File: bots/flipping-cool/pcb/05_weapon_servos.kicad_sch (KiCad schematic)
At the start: 6 parts, among them J30 SAVOX_SH0255MGP_FRONT_REAR_AX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, J31 SAVOX_SH0255MGP_LEFT_RIGHT_AX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, J32 SPARE_SERVO_PWM5, J33 SPARE_SERVO_PWM6

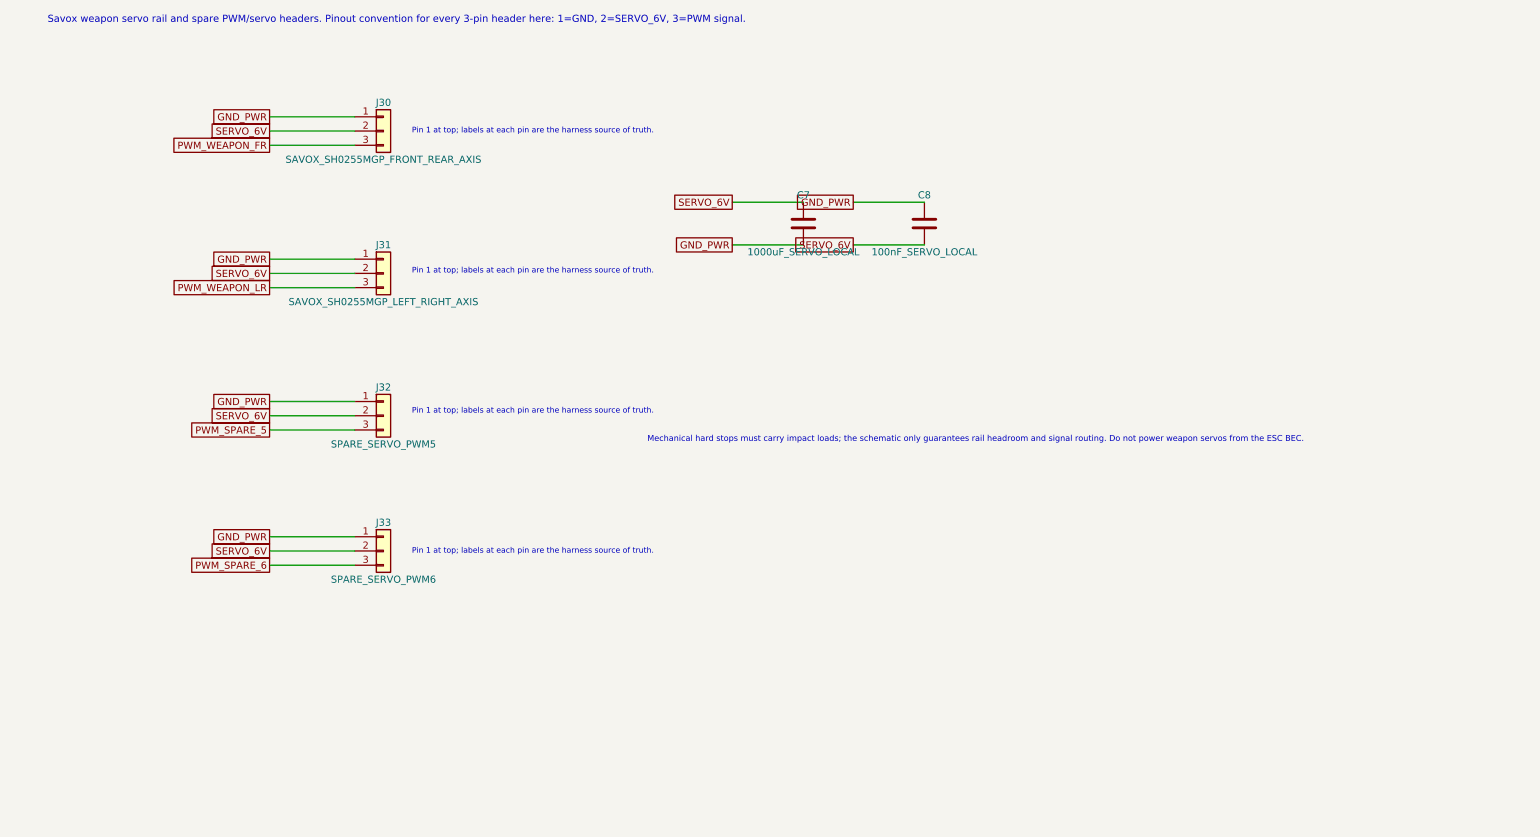
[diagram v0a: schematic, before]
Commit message: Refactor Flipping Cool PCB design to Rev B, updating title, date, and revision details. Integrate ESP32-S3 module and enhance documentation for MCU I/O and debugging features, while maintaining historical context from Rev A.
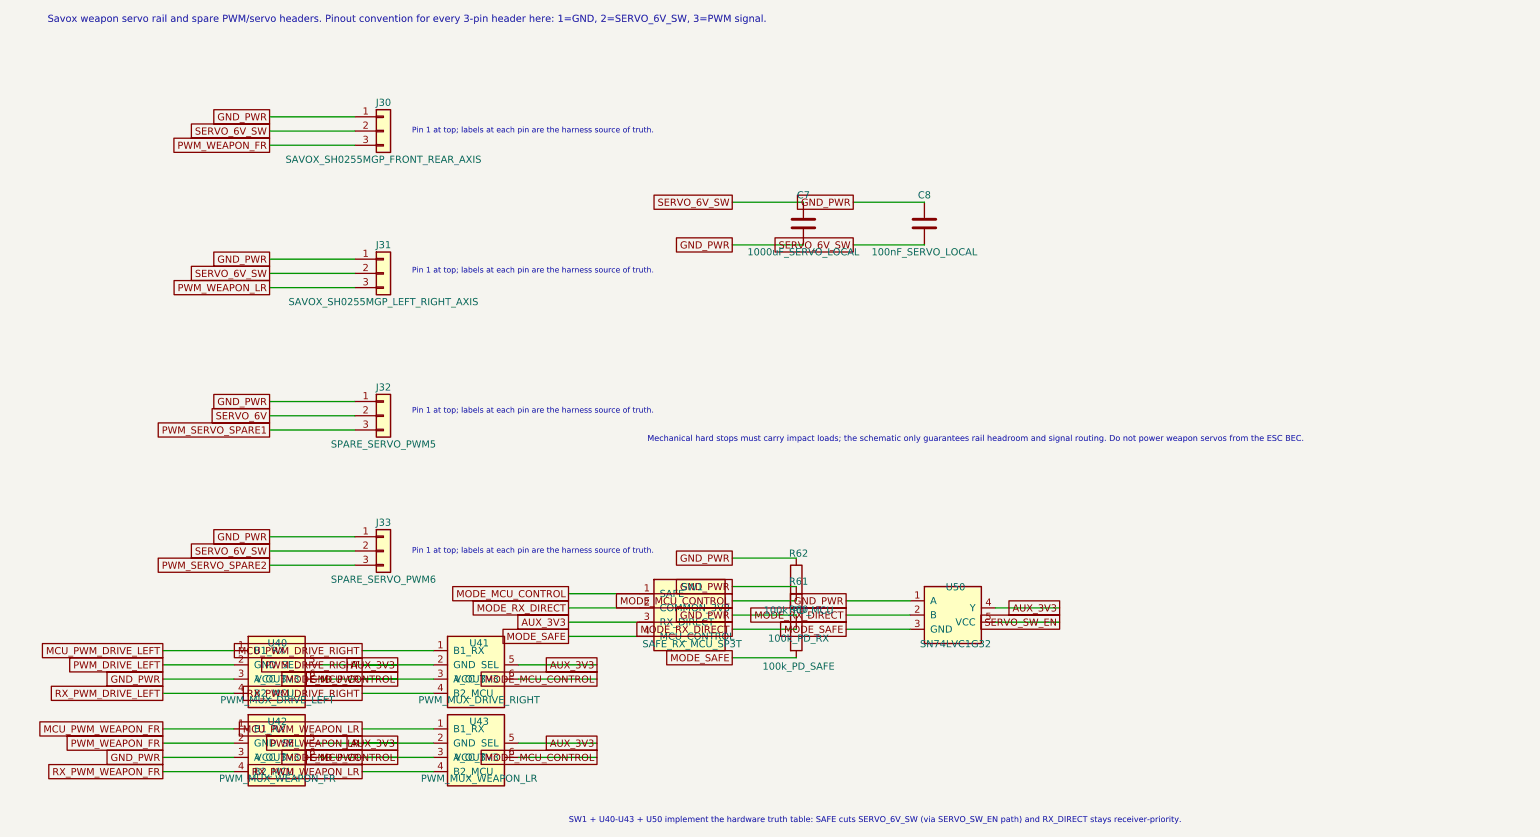
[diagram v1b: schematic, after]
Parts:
- added R60: 100k_PD_SAFE, Resistor_SMD:R_0805_2012Metric, symbol Device:R
- added R61: 100k_PD_RX, Resistor_SMD:R_0805_2012Metric, symbol Device:R
- added R62: 100k_PD_MCU, Resistor_SMD:R_0805_2012Metric, symbol Device:R
- added SW1: SAFE_RX_MCU_SP3T, Button_Switch_SMD:SW_SP3T_PCM13, symbol custom:MODE_SWITCH_SP3T_SAFE_RX_MCU
- added U40: PWM_MUX_DRIVE_LEFT, Package_TO_SOT_SMD:SOT-23-6, symbol custom:MUX_74LVC1G3157
- added U41: PWM_MUX_DRIVE_RIGHT, Package_TO_SOT_SMD:SOT-23-6, symbol custom:MUX_74LVC1G3157
- added U42: PWM_MUX_WEAPON_FR, Package_TO_SOT_SMD:SOT-23-6, symbol custom:MUX_74LVC1G3157
- added U43: PWM_MUX_WEAPON_LR, Package_TO_SOT_SMD:SOT-23-6, symbol custom:MUX_74LVC1G3157
- added U50: SN74LVC1G32, Package_TO_SOT_SMD:SOT-23-5, symbol custom:LOGIC_SN74LVC1G32
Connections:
- net GND_PWR: now also R60.1, R61.1, R62.1, R62.2, SW1.1 (SAFE), U40.3 (A_OUT), U40.6 (VCC_3V3), U41.3 (A_OUT), U41.6 (VCC_3V3), U42.3 (A_OUT), U42.6 (VCC_3V3), U43.3 (A_OUT), U43.6 (VCC_3V3), U50.1 (A)
- net PWM_WEAPON_FR: now also U42.2 (GND)
- net SERVO_6V: no longer C7.1, C8.2, J30.2 (Pin_2), J31.2 (Pin_2), J33.2 (Pin_2)
- net PWM_SPARE_5 renamed PWM_SERVO_SPARE1
- net PWM_SPARE_6 renamed PWM_SERVO_SPARE2
- net PWM_WEAPON_LR renamed AUX_3V3
- net AUX_3V3: now also SW1.3 (RX_DIRECT), U40.5 (SEL), U41.2 (GND), U41.5 (SEL), U42.5 (SEL), U43.2 (GND), U43.5 (SEL), U50.4 (Y)
- new net MCU_PWM_DRIVE_LEFT: U40.1 (B1_RX)
- new net MCU_PWM_DRIVE_RIGHT: U41.1 (B1_RX)
- new net MCU_PWM_WEAPON_FR: U42.1 (B1_RX)
- new net MCU_PWM_WEAPON_LR: U43.1 (B1_RX)
- new net MODE_RX_DIRECT: R61.2, SW1.2 (COMMON_3V3), U50.2 (B)
- new net MODE_SAFE: R60.2, SW1.4 (MCU_CONTROL), U50.3 (GND)
- new net PWM_DRIVE_LEFT: U40.2 (GND)
- new net RX_PWM_DRIVE_LEFT: U40.4 (B2_MCU)
- new net RX_PWM_DRIVE_RIGHT: U41.4 (B2_MCU)
- new net RX_PWM_WEAPON_FR: U42.4 (B2_MCU)
- new net RX_PWM_WEAPON_LR: U43.4 (B2_MCU)
- new net SERVO_6V_SW: C7.1, C8.2, J30.2 (Pin_2), J31.2 (Pin_2), J33.2 (Pin_2)
- new net SERVO_SW_EN: U50.5 (VCC)
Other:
- note added: "SW1 + U40-U43 + U50 implement the hardware truth table: SAFE cuts SERVO_6V_SW (via SERVO_SW_EN path) and RX_DIRECT stays receiver-priority."
- note added: "Savox weapon servo rail and spare PWM/servo headers. Pinout convention for every 3-pin header here: 1=GND, 2=SERVO_6V_SW, 3=PWM signal."
- note removed: "Savox weapon servo rail and spare PWM/servo headers. Pinout convention for every 3-pin header here: 1=GND, 2=SERVO_6V, 3=PWM signal."
- title: Flipping Cool Rev A - Weapon Servos -> Flipping Cool Rev B - Authority and Servos

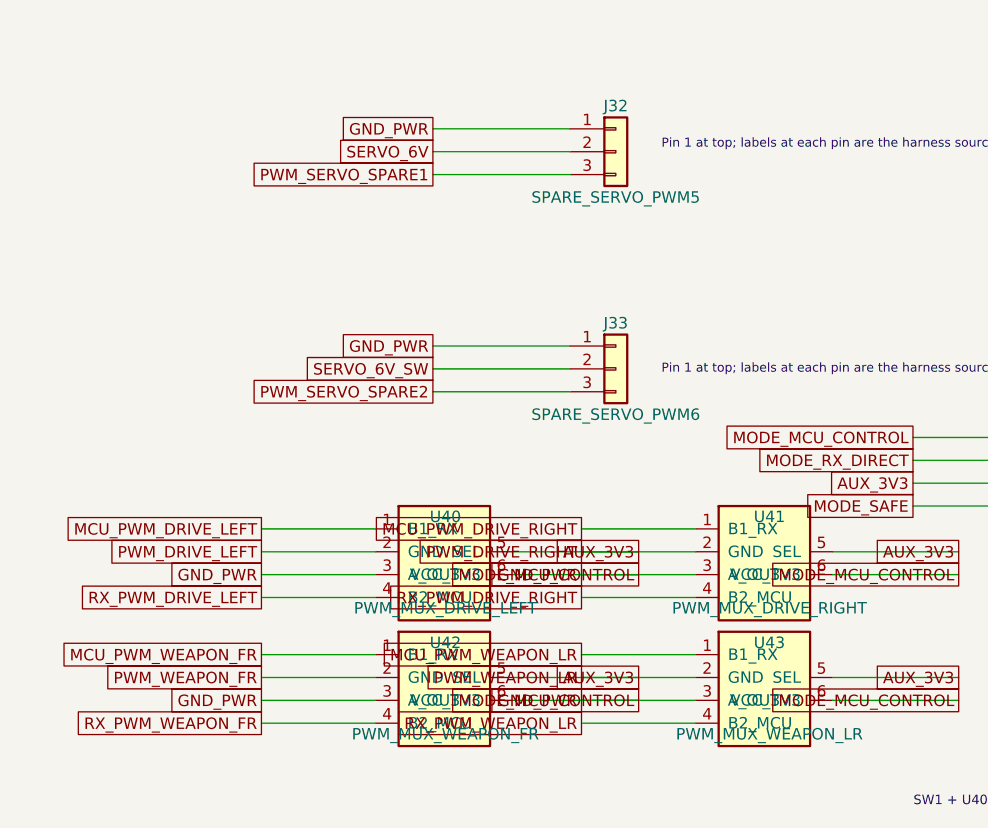
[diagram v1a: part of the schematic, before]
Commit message: Remove obsolete Flipping Cool Rev B project plan file and update schematic files to reflect the latest design changes, including integration of the ESP32-S3 module and enhancements to power management and control authority. Ensure all documentation is aligned with the current PCB design and architecture.
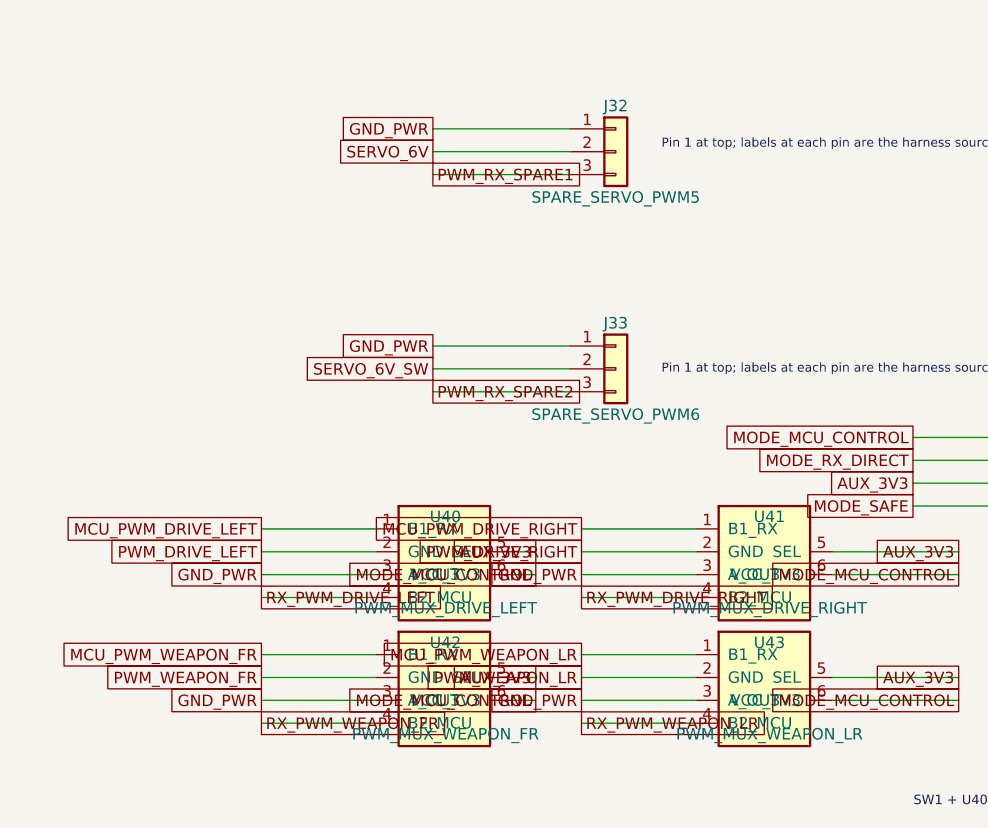
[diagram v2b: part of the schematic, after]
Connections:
- net AUX_3V3: no longer J31.3 (Pin_3), U41.2 (GND), U43.2 (GND)
- net GND_PWR: no longer R62.2, SW1.1 (SAFE), U40.6 (VCC_3V3), U41.6 (VCC_3V3), U42.6 (VCC_3V3), U43.6 (VCC_3V3)
- net PWM_SERVO_SPARE1 renamed PWM_RX_SPARE1
- net PWM_SERVO_SPARE2 renamed PWM_RX_SPARE2
- new net MODE_MCU_CONTROL: R62.2, SW1.1 (SAFE), U40.6 (VCC_3V3), U41.6 (VCC_3V3), U42.6 (VCC_3V3), U43.6 (VCC_3V3)
- new net PWM_DRIVE_RIGHT: U41.2 (GND)
- new net PWM_WEAPON_LR: J31.3 (Pin_3), U43.2 (GND)
